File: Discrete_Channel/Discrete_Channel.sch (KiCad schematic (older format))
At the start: 67 parts, among them J1 Conn_01x05_Male, J2 Conn_01x06_Male, J3 Conn_01x05_Male, J4 Banna Jack, U1 TPA3244, U2 LM4562

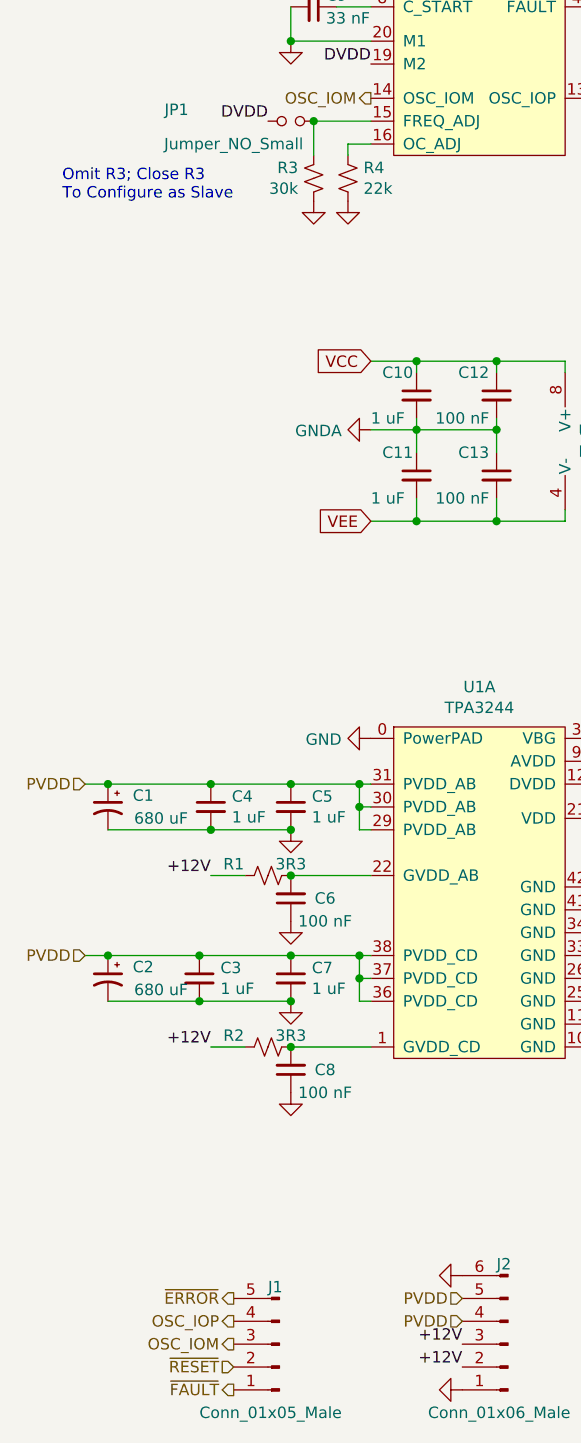
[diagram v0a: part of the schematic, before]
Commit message: Circuit R2
Fixed Issue with heatsink pad shorting out amplifier.
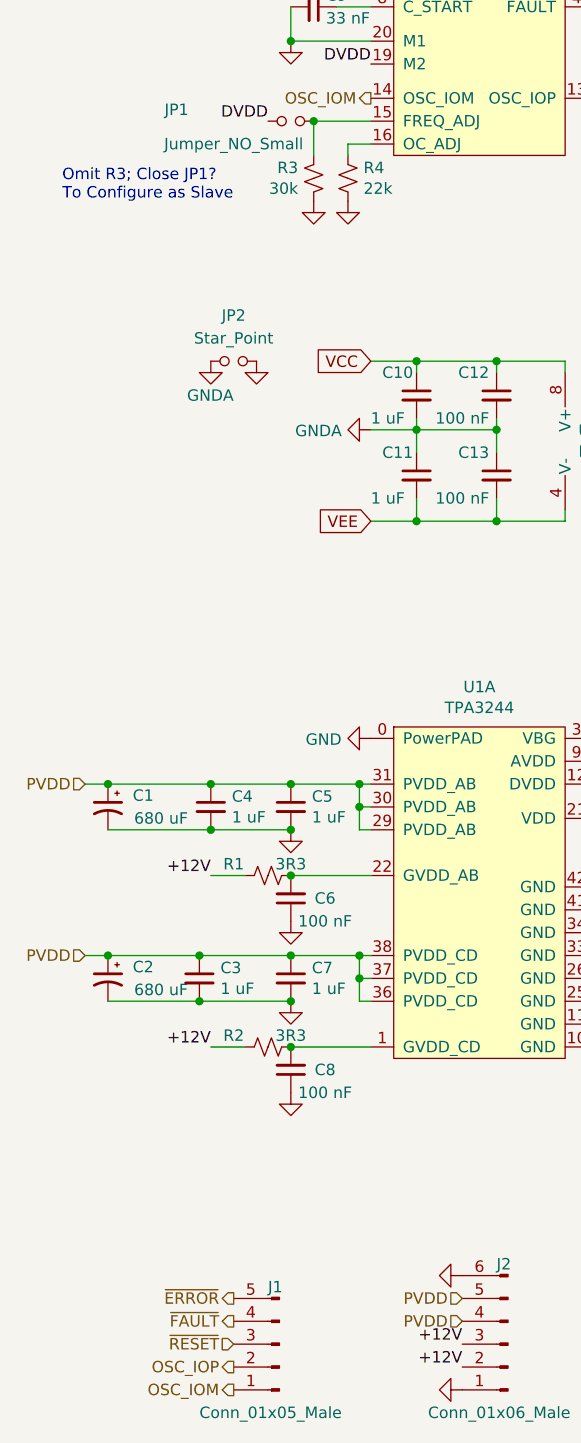
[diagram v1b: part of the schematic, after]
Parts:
- added JP2: Star_Point, Jumper:SolderJumper-2_P1.3mm_Open_Pad1.0x1.5mm, symbol Device:Jumper_NO_Small
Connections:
- net GND: now also JP2.1
- net GNDA: now also JP2.2
- net OSC_IOM: now also J1.1 (Pin_1); no longer J1.3 (Pin_3)
- net OSC_IOP: now also J1.2 (Pin_2); no longer J1.4 (Pin_4)
- net ~FAULT: now also J1.4 (Pin_4); no longer J1.1 (Pin_1)
- net ~RESET: now also J1.3 (Pin_3); no longer J1.2 (Pin_2)
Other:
- note added: "Omit R3; Close JP1?\nTo Configure as Slave"
- note removed: "Omit R3; Close R3\nTo Configure as Slave"
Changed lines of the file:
@@
 Text GLabel 3800 7200 0    50   Input ~ 0
 VEE
-Text HLabel 1800 7300 0    50   Input ~ 0
+Text HLabel 1800 7200 0    50   Input ~ 0
 ~RESET
-Text HLabel 1800 7200 0    50   Output ~ 0
+Text HLabel 1800 7400 0    50   Output ~ 0
 OSC_IOM
+Text HLabel 1800 7300 0    50   Output ~ 0
+OSC_IOP
 Text HLabel 1800 7100 0    50   Output ~ 0
-OSC_IOP
-Text HLabel 1800 7400 0    50   Output ~ 0
 ~FAULT
 Text HLabel 1800 7000 0    50   Output ~ 0
@@
 DVDD
 Text Notes 1050 2200 0    50   ~ 0
-Omit R3; Close R3\nTo Configure as Slave
+Omit R3; Close JP1?\nTo Configure as Slave
+$Comp
+L Device:Jumper_NO_Small JP2
+U 1 1 61E2061A
+P 1800 2900
+F 0 "JP2" H 1800 2700 50  0000 C CNN
+F 1 "Star_Point" H 1800 2800 50  0000 C CNN
+F 2 "Jumper:SolderJumper-2_P1.3mm_Open_Pad1.0x1.5mm" H 1800 2900 50  0001 C CNN
+F 3 "~" H 1800 2900 50  0001 C CNN
+	1    1800 2900
+	-1   0    0    1
+$EndComp
+$Comp
+L power:GND #PWR0104
+U 1 1 61E2223B
+P 1900 2900
+F 0 "#PWR0104" H 1900 2650 50  0001 C CNN
+F 1 "GND" H 1900 2750 50  0001 C CNN
+F 2 "" H 1900 2900 50  0001 C CNN
+F 3 "" H 1900 2900 50  0001 C CNN
+	1    1900 2900
+	1    0    0    -1
+$EndComp
+$Comp
+L power:GNDA #PWR0105
+U 1 1 61E23DCD
+P 1700 2900
+F 0 "#PWR0105" H 1700 2650 50  0001 C CNN
+F 1 "GNDA" H 1800 2750 50  0000 R CNN
+F 2 "" H 1700 2900 50  0001 C CNN
+F 3 "" H 1700 2900 50  0001 C CNN
+	1    1700 2900
+	1    0    0    -1
+$EndComp
 $EndSCHEMATC
